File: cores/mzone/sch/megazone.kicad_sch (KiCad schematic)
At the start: 8 parts

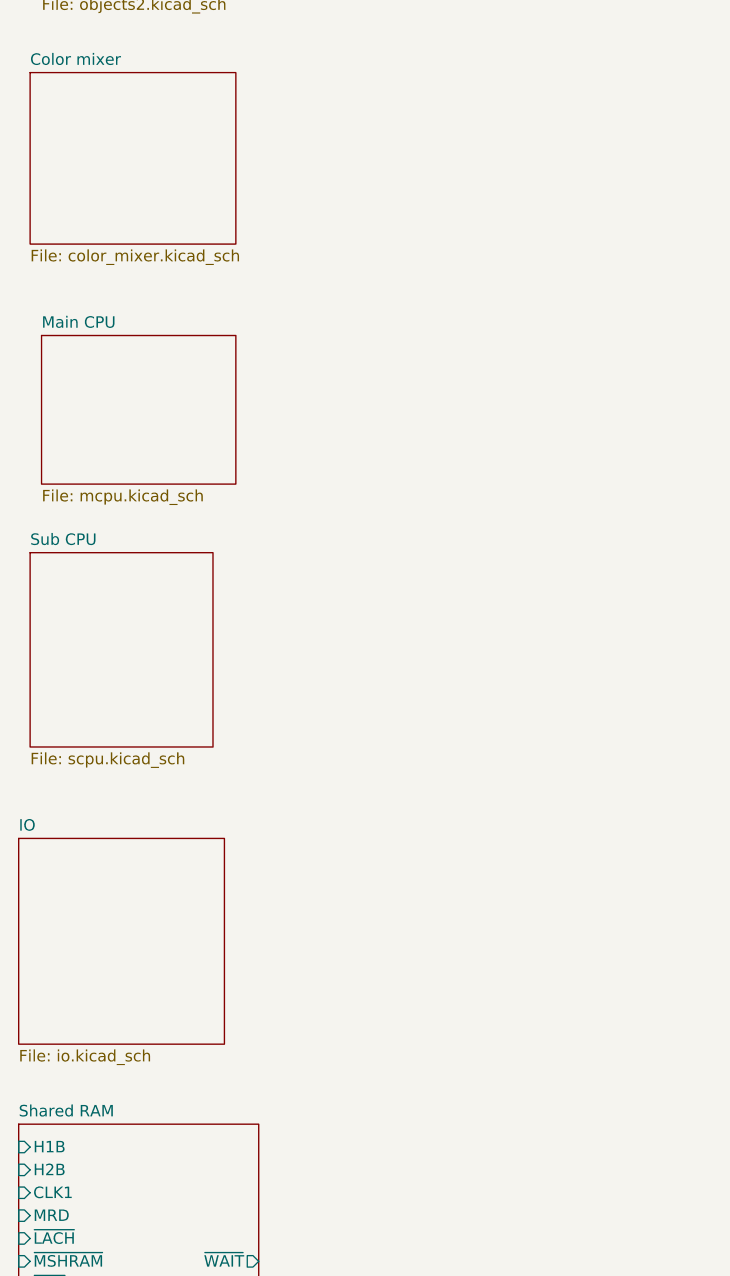
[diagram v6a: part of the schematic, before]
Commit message: mzone core
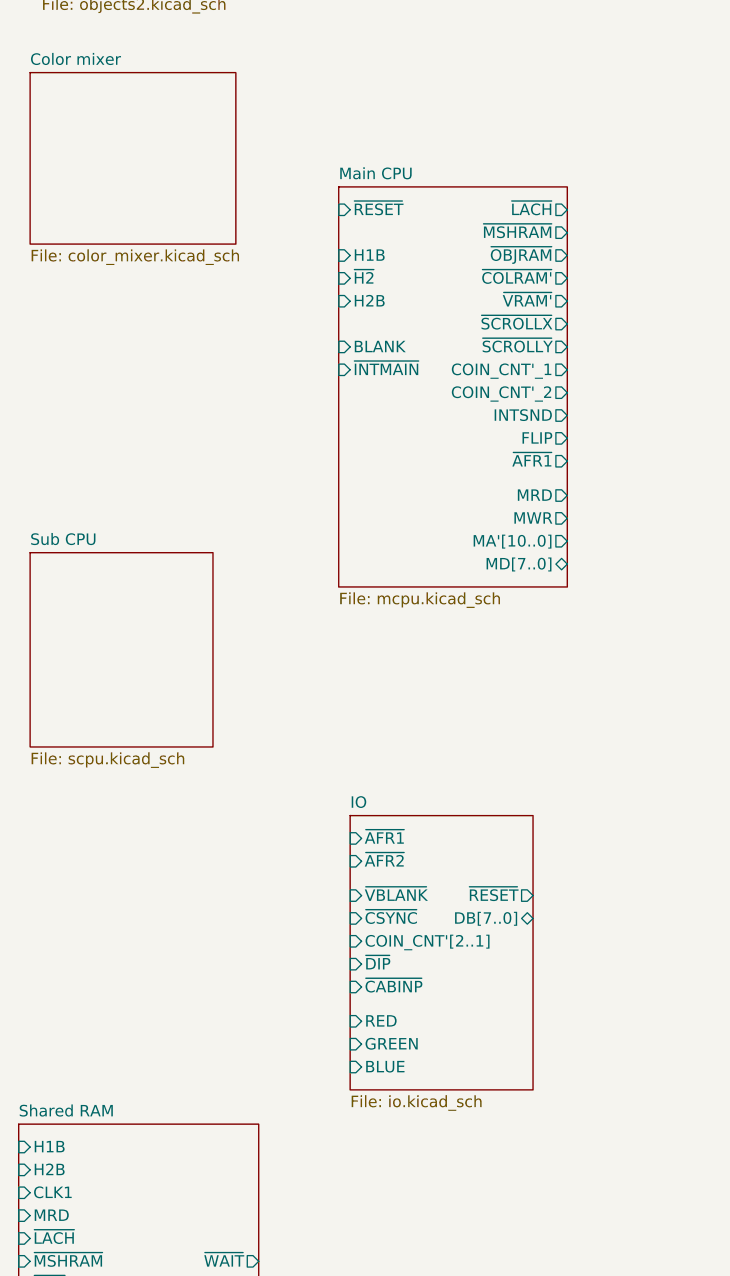
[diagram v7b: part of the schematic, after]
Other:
- sheet IO ports: added BLUE, COIN_CNT'[2..1], DB[7..0], GREEN, RED, ~{AFR1}, ~{AFR2}, ~{CABINP}, ~{CSYNC}, ~{DIP}, ~{RESET}, ~{VBLANK}; removed none
- sheet Main CPU ports: added BLANK, COIN_CNT'_1, COIN_CNT'_2, FLIP, H1B, H2B, INTSND, MA'[10..0], MD[7..0], MRD, MWR, ~{AFR1}, ~{COLRAM'}, ~{H2}, ~{INTMAIN}, ~{LACH}, ~{MSHRAM}, ~{OBJRAM}, ~{RESET}, ~{SCROLLX}, ~{SCROLLY}, ~{VRAM'}; removed none

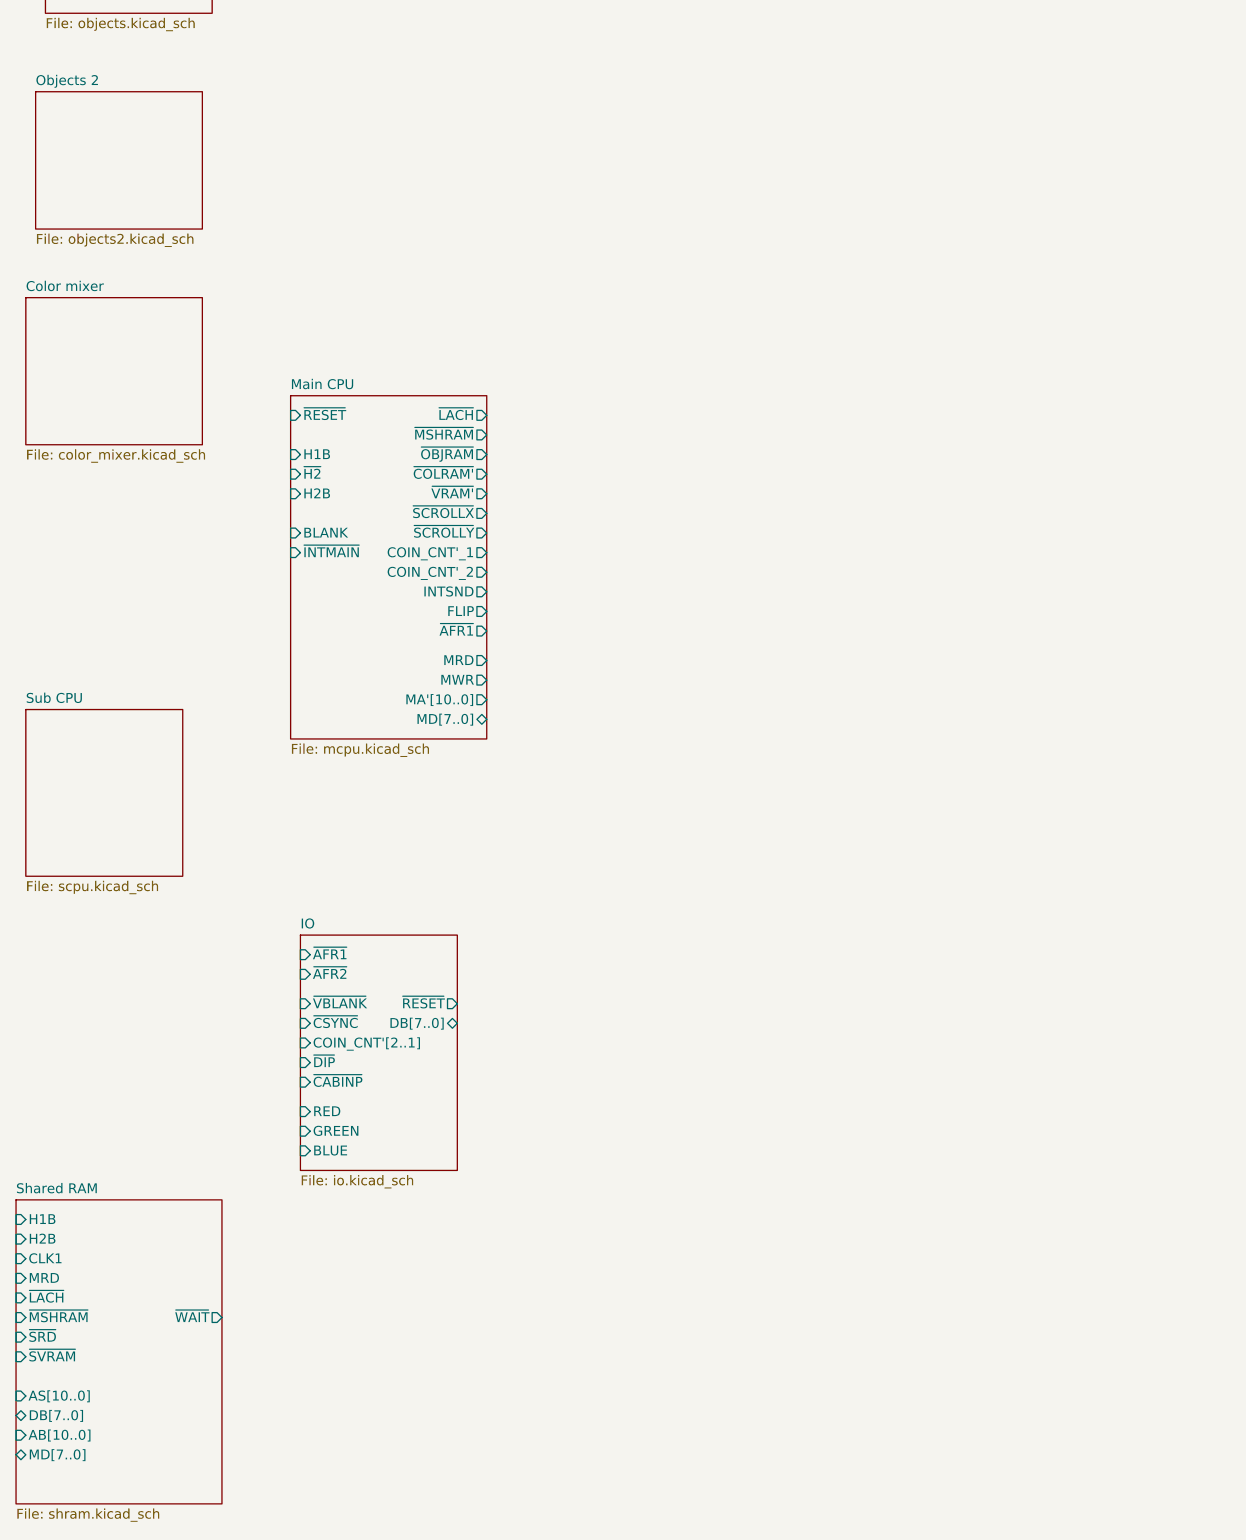
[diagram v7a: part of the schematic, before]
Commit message: mzone core
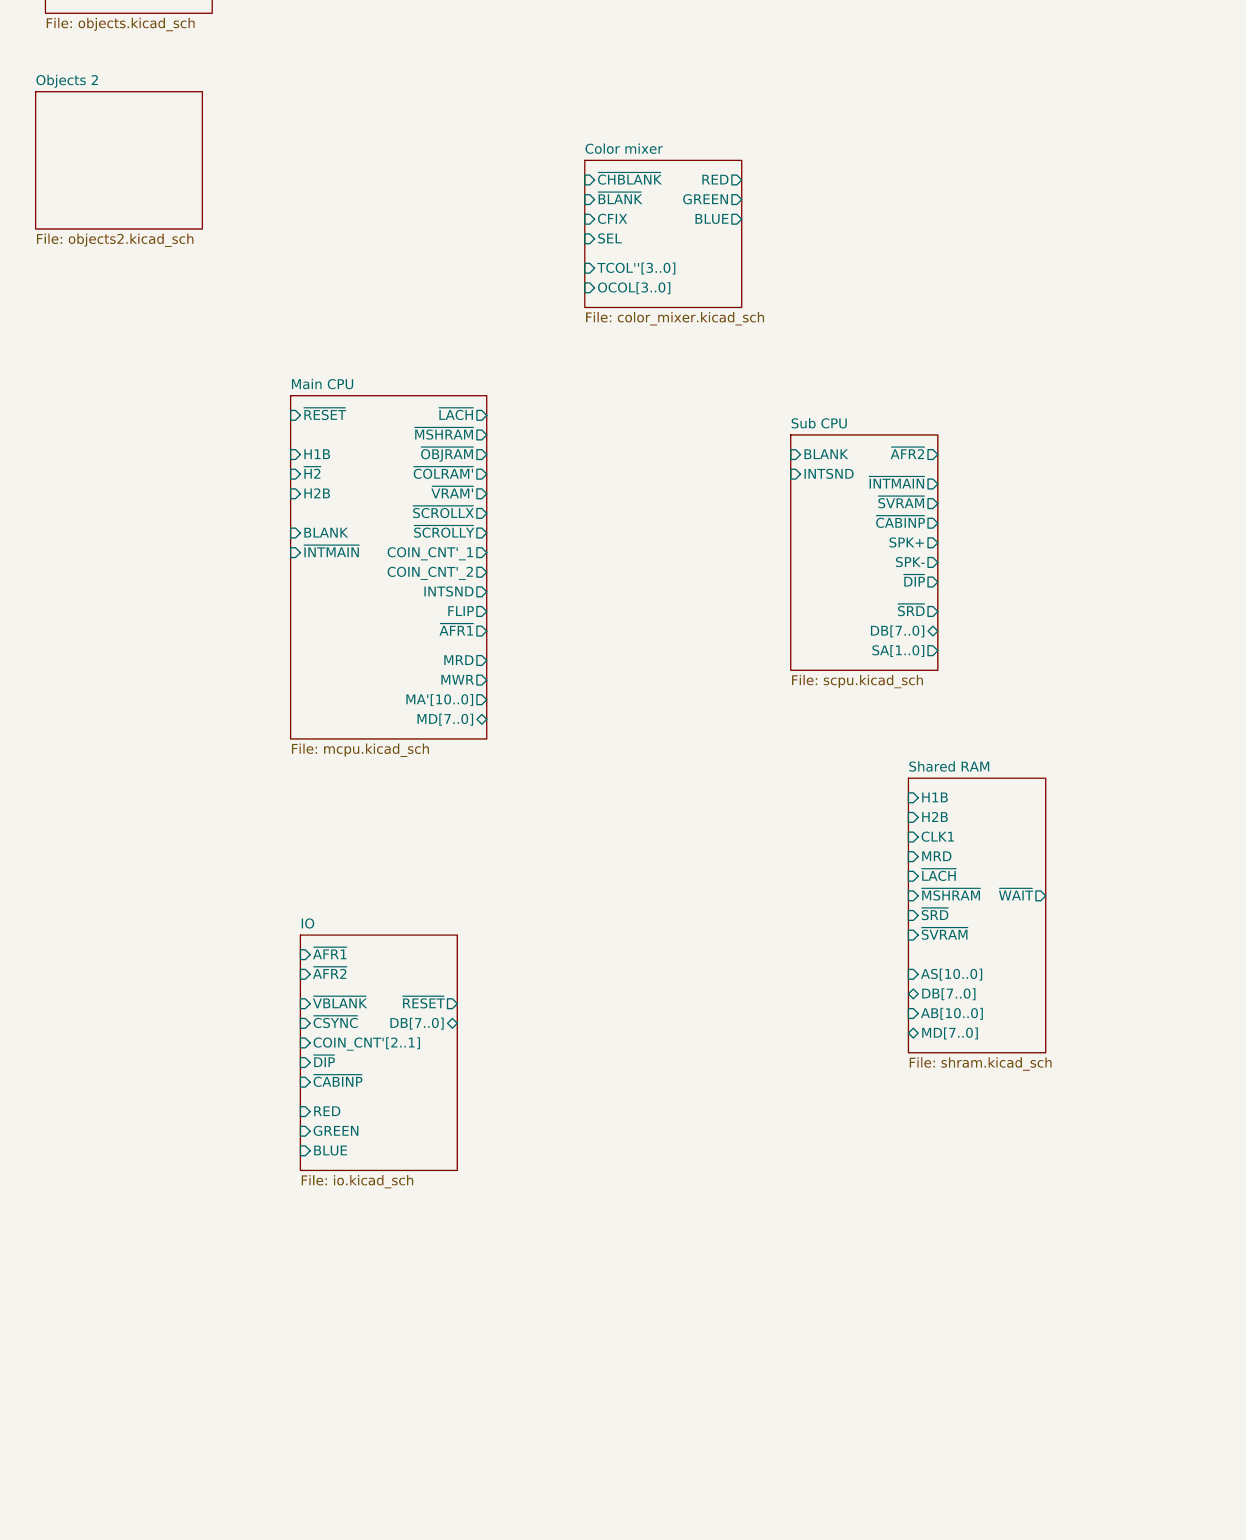
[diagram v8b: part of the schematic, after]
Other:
- sheet Color mixer ports: added BLUE, CFIX, GREEN, OCOL[3..0], RED, SEL, TCOL''[3..0], ~{BLANK}, ~{CHBLANK}; removed none
- sheet Sub CPU ports: added BLANK, DB[7..0], INTSND, SA[1..0], SPK+, SPK-, ~{AFR2}, ~{CABINP}, ~{DIP}, ~{INTMAIN}, ~{SRD}, ~{SVRAM}; removed none
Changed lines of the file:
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@@
 	)
 	(sheet
-		(at 24.13 132.08)
-		(size 22.86 19.05)
+		(at 96.52 114.3)
+		(size 20.32 19.05)
 		(fields_autoplaced yes)
 		(stroke
@@
 		)
 		(property "Sheetname" "Color mixer"
-			(at 24.13 131.3684 0)
+			(at 96.52 113.5884 0)
 			(effects
 				(font
@@
 		)
 		(property "Sheetfile" "color_mixer.kicad_sch"
-			(at 24.13 151.7146 0)
+			(at 96.52 133.9346 0)
 			(effects
 				(font
@@
 				)
 				(justify left top)
+			)
+		)
+		(pin "OCOL[3..0]" input
+			(at 96.52 130.81 180)
+			(effects
+				(font
+					(size 1.27 1.27)
+				)
+				(justify left)
+			)
+		)
+		(pin "TCOL''[3..0]" input
+			(at 96.52 128.27 180)
+			(effects
+				(font
+					(size 1.27 1.27)
+				)
+				(justify left)
+			)
+		)
+		(pin "SEL" input
+			(at 96.52 124.46 180)
+			(effects
+				(font
+					(size 1.27 1.27)
+				)
+				(justify left)
+			)
+		)
+		(pin "~{BLANK}" input
+			(at 96.52 119.38 180)
+			(effects
+				(font
+					(size 1.27 1.27)
+				)
+				(justify left)
+			)
+		)
+		(pin "CFIX" input
+			(at 96.52 121.92 180)
+			(effects
+				(font
+					(size 1.27 1.27)
+				)
+				(justify left)
+			)
+		)
+		(pin "~{CHBLANK}" input
+			(at 96.52 116.84 180)
+			(effects
+				(font
+					(size 1.27 1.27)
+				)
+				(justify left)
+			)
+		)
+		(pin "RED" output
+			(at 116.84 116.84 0)
+			(effects
+				(font
+					(size 1.27 1.27)
+				)
+				(justify right)
+			)
+		)
+		(pin "GREEN" output
+			(at 116.84 119.38 0)
+			(effects
+				(font
+					(size 1.27 1.27)
+				)
+				(justify right)
+			)
+		)
+		(pin "BLUE" output
+			(at 116.84 121.92 0)
+			(effects
+				(font
+					(size 1.27 1.27)
+				)
+				(justify right)
 			)
 		)
@@
 	)
 	(sheet
-		(at 22.86 248.92)
-		(size 26.67 39.37)
+		(at 138.43 194.31)
+		(size 17.78 35.56)
 		(fields_autoplaced yes)
 		(stroke
@@
 		)
 		(property "Sheetname" "Shared RAM"
-			(at 22.86 248.2084 0)
+			(at 138.43 193.5984 0)
 			(effects
 				(font
@@
 		)
 		(property "Sheetfile" "shram.kicad_sch"
-			(at 22.86 288.8746 0)
+			(at 138.43 230.4546 0)
 			(effects
 				(font
@@
 		)
 		(pin "H2B" input
-			(at 22.86 254 180)
+			(at 138.43 199.39 180)
 			(effects
 				(font
@@
 		)
 		(pin "MRD" input
-			(at 22.86 259.08 180)
+			(at 138.43 204.47 180)
 			(effects
 				(font
@@
 		)
 		(pin "~{LACH}" input
-			(at 22.86 261.62 180)
+			(at 138.43 207.01 180)
 			(effects
 				(font
@@
 		)
 		(pin "~{MSHRAM}" input
-			(at 22.86 264.16 180)
+			(at 138.43 209.55 180)
 			(effects
 				(font
@@
 		)
 		(pin "H1B" input
-			(at 22.86 251.46 180)
+			(at 138.43 196.85 180)
 			(effects
 				(font
@@
 		)
 		(pin "~{WAIT}" output
-			(at 49.53 264.16 0)
+			(at 156.21 209.55 0)
 			(effects
 				(font
@@
 		)
 		(pin "DB[7..0]" bidirectional
-			(at 22.86 276.86 180)
+			(at 138.43 222.25 180)
 			(effects
 				(font
@@
 		)
 		(pin "~{SRD}" input
-			(at 22.86 266.7 180)
+			(at 138.43 212.09 180)
 			(effects
 				(font
@@
 		)
 		(pin "~{SVRAM}" input
-			(at 22.86 269.24 180)
+			(at 138.43 214.63 180)
 			(effects
 				(font
@@
 		)
 		(pin "CLK1" input
-			(at 22.86 256.54 180)
+			(at 138.43 201.93 180)
 			(effects
 				(font
@@
 		)
 		(pin "AB[10..0]" input
-			(at 22.86 279.4 180)
+			(at 138.43 224.79 180)
 			(effects
 				(font
@@
 		)
 		(pin "MD[7..0]" bidirectional
-			(at 22.86 281.94 180)
+			(at 138.43 227.33 180)
 			(effects
 				(font
@@
 		)
 		(pin "AS[10..0]" input
-			(at 22.86 274.32 180)
+			(at 138.43 219.71 180)
 			(effects
 				(font
@@
 	)
 	(sheet
-		(at 24.13 185.42)
-		(size 20.32 21.59)
+		(at 123.19 149.86)
+		(size 19.05 30.48)
 		(fields_autoplaced yes)
 		(stroke
@@
 		)
 		(property "Sheetname" "Sub CPU"
-			(at 24.13 184.7084 0)
+			(at 123.19 149.1484 0)
 			(effects
 				(font
@@
 		)
 		(property "Sheetfile" "scpu.kicad_sch"
-			(at 24.13 207.5946 0)
+			(at 123.19 180.9246 0)
 			(effects
 				(font
@@
 			)
 		)
+		(pin "SPK-" output
+			(at 142.24 166.37 0)
+			(effects
+				(font
+					(size 1.27 1.27)
+				)
+				(justify right)
+			)
+		)
+		(pin "SPK+" output
+			(at 142.24 163.83 0)
+			(effects
+				(font
+					(size 1.27 1.27)
+				)
+				(justify right)
+			)
+		)
+		(pin "~{DIP}" output
+			(at 142.24 168.91 0)
+			(effects
+				(font
+					(size 1.27 1.27)
+				)
+				(justify right)
+			)
+		)
+		(pin "~{SVRAM}" output
+			(at 142.24 158.75 0)
+			(effects
+				(font
+					(size 1.27 1.27)
+				)
+				(justify right)
+			)
+		)
+		(pin "~{CABINP}" output
+			(at 142.24 161.29 0)
+			(effects
+				(font
+					(size 1.27 1.27)
+				)
+				(justify right)
+			)
+		)
+		(pin "~{AFR2}" output
+			(at 142.24 152.4 0)
+			(effects
+				(font
+					(size 1.27 1.27)
+				)
+				(justify right)
+			)
+		)
+		(pin "~{INTMAIN}" output
+			(at 142.24 156.21 0)
+			(effects
+				(font
+					(size 1.27 1.27)
+				)
+				(justify right)
+			)
+		)
+		(pin "~{SRD}" output
+			(at 142.24 172.72 0)
+			(effects
+				(font
+					(size 1.27 1.27)
+				)
+				(justify right)
+			)
+		)
+		(pin "DB[7..0]" bidirectional
+			(at 142.24 175.26 0)
+			(effects
+				(font
+					(size 1.27 1.27)
+				)
+				(justify right)
+			)
+		)
+		(pin "SA[1..0]" output
+			(at 142.24 177.8 0)
+			(effects
+				(font
+					(size 1.27 1.27)
+				)
+				(justify right)
+			)
+		)
+		(pin "BLANK" input
+			(at 123.19 152.4 180)
+			(effects
+				(font
+					(size 1.27 1.27)
+				)
+				(justify left)
+			)
+		)
+		(pin "INTSND" input
+			(at 123.19 154.94 180)
+			(effects
+				(font
+					(size 1.27 1.27)
+				)
+				(justify left)
+			)
+		)
